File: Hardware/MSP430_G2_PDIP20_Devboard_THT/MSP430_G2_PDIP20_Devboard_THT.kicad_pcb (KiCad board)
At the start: 2 copper layers, 69 x 36 mm, 32 parts, among them J1 2479774-1, J2 Conn_01x04_Pin, J3 Conn_01x10_Pin, J4 Conn_01x10_Pin, SW1 SW_RESET, U1 MSP430G2302IN20, U2 AP2112K-3.3TRG1(MS), U3 PESD5V0S1BA_C5261083

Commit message: MSP430 G2 PDIP20 Dev Board - Layout - Added JLCPCB Design Rules
Signed-off-by: alexanderjg85 <alexanderjg85@gmail.com>
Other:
- rule pad_to_mask_clearance: 0 -> 0.05
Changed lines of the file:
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@@
 		(33 "B.Fab" user)
 		(39 "User.1" user)
-		(41 "User.2" user)
-		(43 "User.3" user)
-		(45 "User.4" user)
 	)
 	(setup
-		(pad_to_mask_clearance 0)
+		(stackup
+			(layer "F.SilkS"
+				(type "Top Silk Screen")
+			)
+			(layer "F.Paste"
+				(type "Top Solder Paste")
+			)
+			(layer "F.Mask"
+				(type "Top Solder Mask")
+				(thickness 0.01)
+			)
+			(layer "F.Cu"
+				(type "copper")
+				(thickness 0.035)
+			)
+			(layer "dielectric 1"
+				(type "core")
+				(thickness 1.51)
+				(material "FR4")
+				(epsilon_r 4.5)
+				(loss_tangent 0.02)
+			)
+			(layer "B.Cu"
+				(type "copper")
+				(thickness 0.035)
+			)
+			(layer "B.Mask"
+				(type "Bottom Solder Mask")
+				(thickness 0.01)
+			)
+			(layer "B.Paste"
+				(type "Bottom Solder Paste")
+			)
+			(layer "B.SilkS"
+				(type "Bottom Silk Screen")
+			)
+			(copper_finish "HAL SnPb")
+			(dielectric_constraints no)
+		)
+		(pad_to_mask_clearance 0.05)
+		(solder_mask_min_width 0.1)
 		(allow_soldermask_bridges_in_footprints no)
 		(tenting
-			(front yes)
-			(back yes)
+			(front no)
+			(back no)
 		)
 		(covering
@@
 		(capping no)
 		(filling no)
+		(zone_defaults)
 		(pcbplotparams
 			(layerselection 0x00000000_00000000_55555555_5755f5ff)

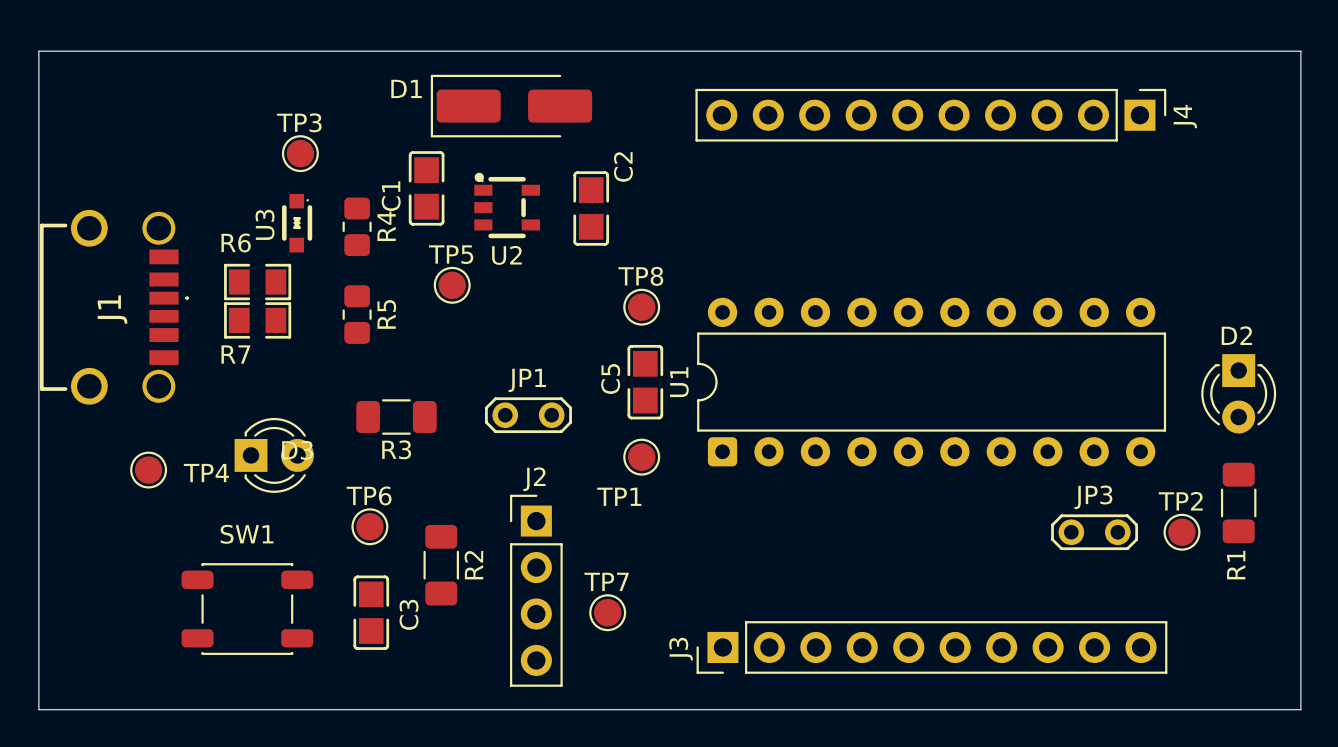
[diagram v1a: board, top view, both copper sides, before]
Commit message: MSP430 G2 PDIP20 Dev Board - Layout - Initial Routing done
Signed-off-by: alexanderjg85 <alexanderjg85@gmail.com>
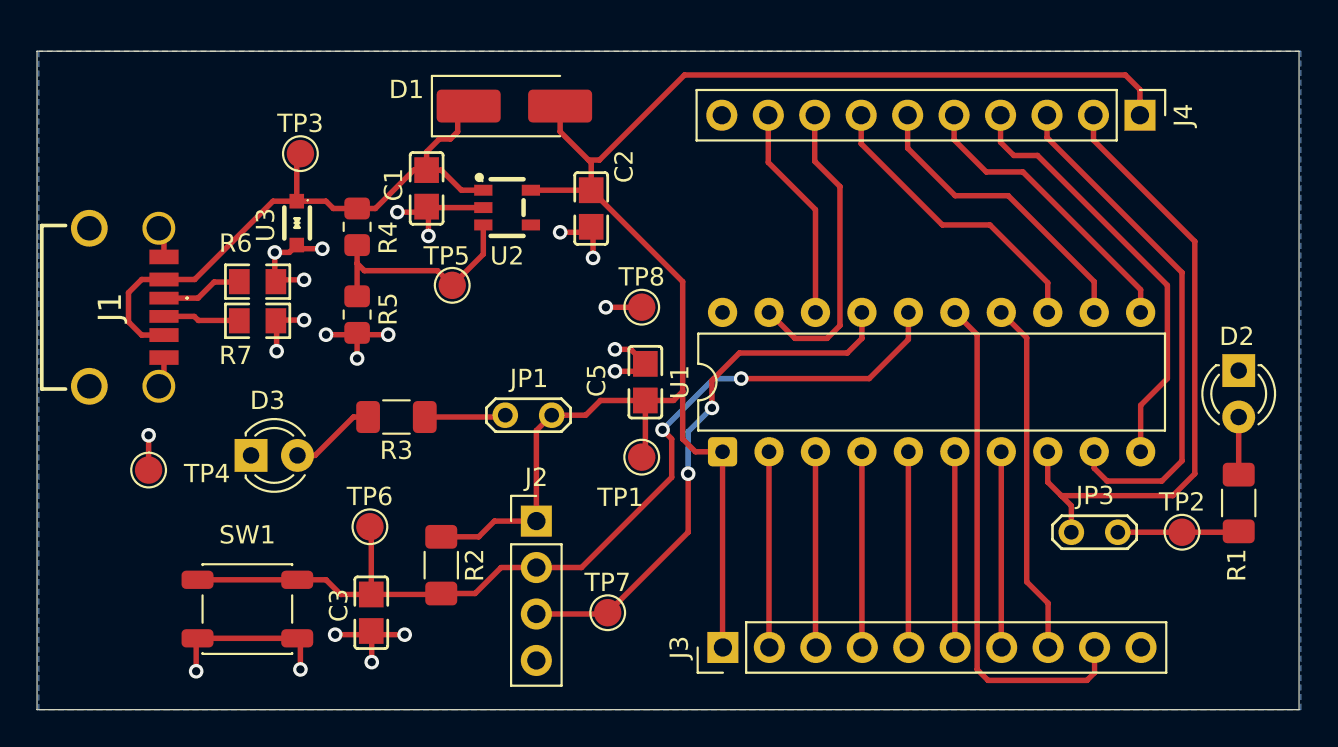
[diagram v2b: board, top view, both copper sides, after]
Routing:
- net VDD: track 0.00 -> 93.8 mm
- net MSP_RST: track 0.00 -> 52.4 mm, vias 0 -> 2
- net GND: track 0.00 -> 50.0 mm, vias 0 -> 21
- net MSP_LED: track 0.00 -> 34.6 mm
- net VCC: track 0.00 -> 34.3 mm
- net MSP_TEST: track 0.00 -> 29.6 mm, vias 0 -> 2
- net /P2.1: track 0.00 -> 28.4 mm
- net /P1.7: track 0.00 -> 28.2 mm
- net /P2.2: track 0.00 -> 23.5 mm
- net /P1.6: track 0.00 -> 19.4 mm
- net /P2.6: track 0.00 -> 16.8 mm
- net /P2.4: track 0.00 -> 16.7 mm
- net /P2.5: track 0.00 -> 16.5 mm
- net /P2.3: track 0.00 -> 16.2 mm
- net Net-(U2-EN): track 0.00 -> 12.5 mm
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- added copper zone on B.Cu, net GND

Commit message: MSP430 G2 PDIP20 Dev Board - Layout - Added Mounting Holes
Signed-off-by: alexanderjg85 <alexanderjg85@gmail.com>
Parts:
- added REF**: MountingHole_2.7mm_M2.5, MountingHole:MountingHole_2.7mm_M2.5, F.Cu at (95.9, 113.6)
- added REF**: MountingHole_2.7mm_M2.5, MountingHole:MountingHole_2.7mm_M2.5, F.Cu at (157.7, 142.4)
- added REF**: MountingHole_2.7mm_M2.5, MountingHole:MountingHole_2.7mm_M2.5, F.Cu at (157.7, 113.6)
- added REF**: MountingHole_2.7mm_M2.5, MountingHole:MountingHole_2.7mm_M2.5, F.Cu at (95.9, 142.4)
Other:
- outline, holes or cut-outs redrawn
- board text added: "Alexander Jaeger 2026"
- board text added: "MSP430G2 PDIP20 Devboard V1 THT"

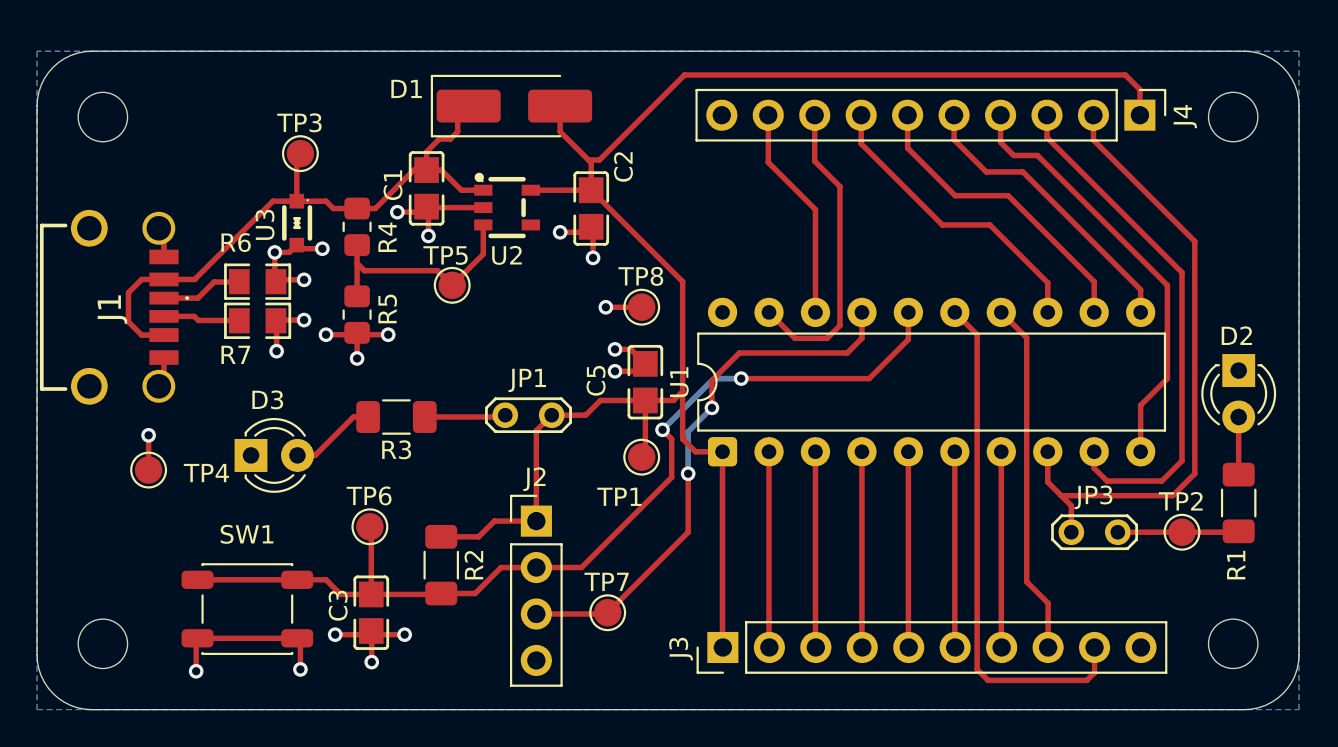
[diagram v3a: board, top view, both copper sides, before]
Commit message: MSP430 G2 PDIP20 Dev Board - Layout - Finished Silk Screen
Signed-off-by: alexanderjg85 <alexanderjg85@gmail.com>
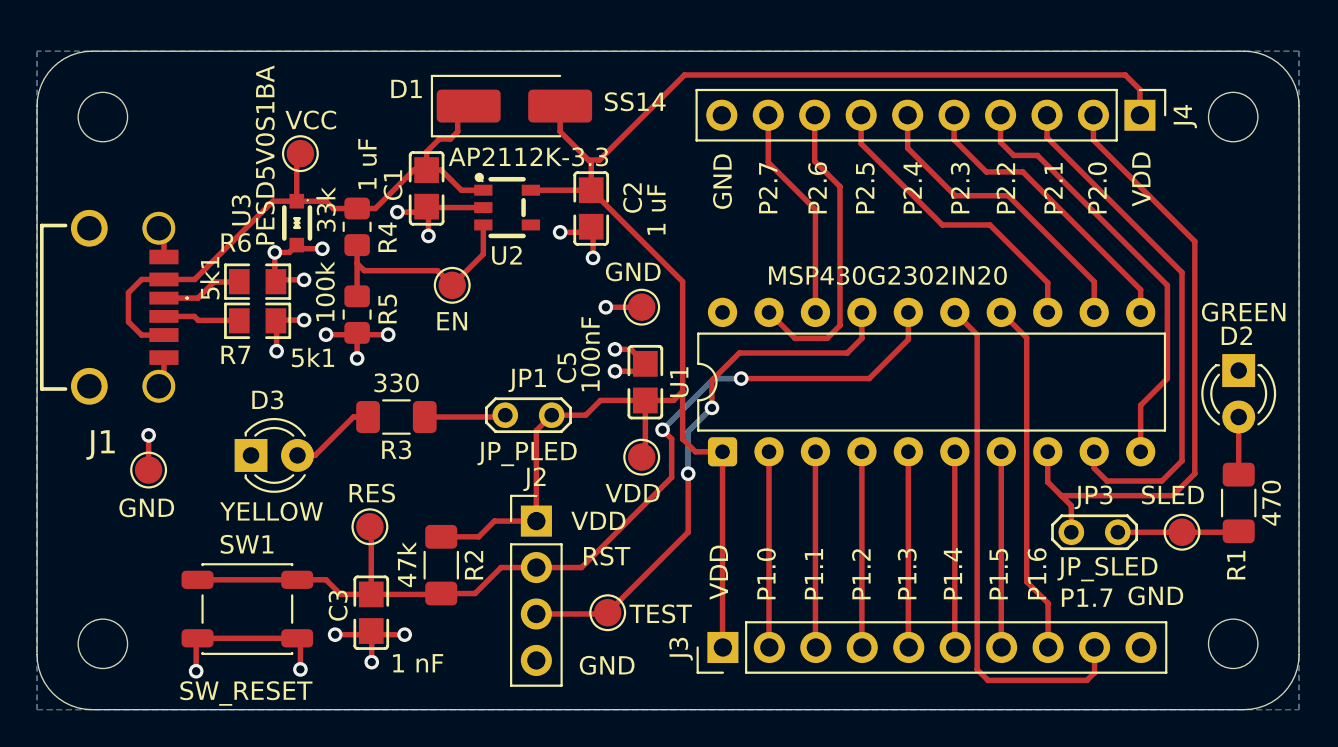
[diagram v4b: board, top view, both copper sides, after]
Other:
- board text added: "AP2112K-3.3"
- board text added: "GND"
- board text added: "P1.0"
- board text added: "P1.1"
- board text added: "P1.2"
- board text added: "P1.3"
- board text added: "P1.4"
- board text added: "P1.5"
- board text added: "P1.6"
- board text added: "P1.7"
- board text added: "P2.0"
- board text added: "P2.1"
- board text added: "P2.2"
- board text added: "P2.3"
- board text added: "P2.4"
- board text added: "P2.5"
- board text added: "P2.6"
- board text added: "P2.7"
- board text added: "PESD5V0S1BA"
- board text added: "RST"
- board text added: "VDD"
